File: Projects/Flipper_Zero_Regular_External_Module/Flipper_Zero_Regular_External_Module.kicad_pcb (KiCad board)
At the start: 2 copper layers, 67.5 x 19.8 mm, 2 parts, among them J1 Flipper_Zero

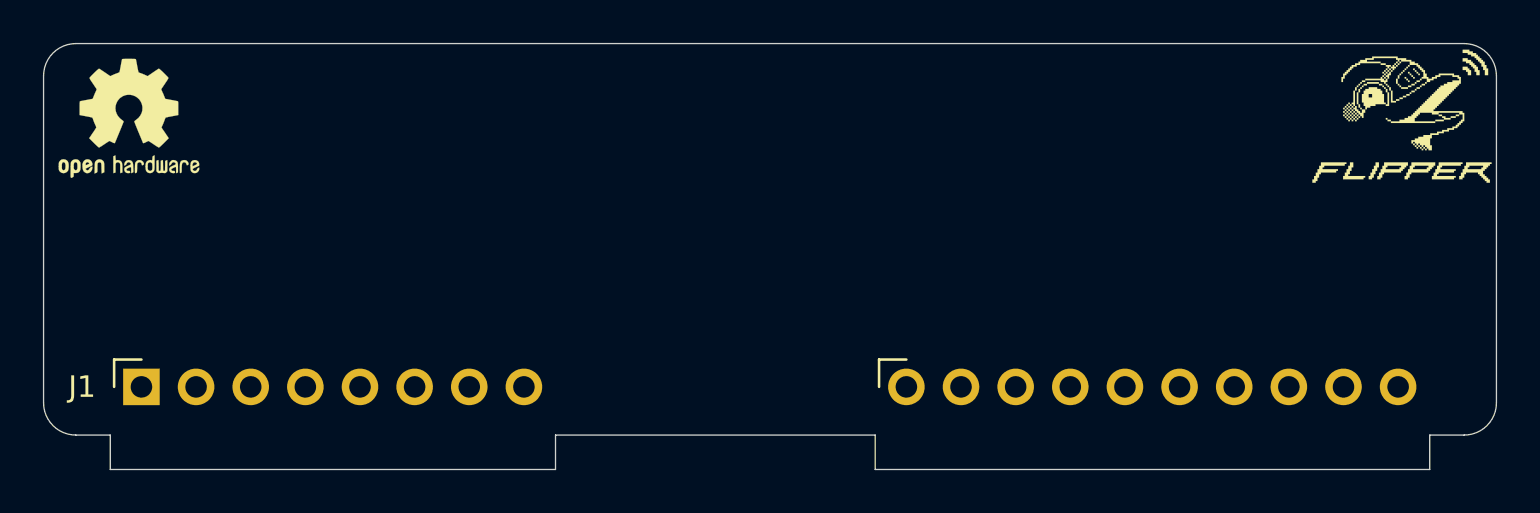
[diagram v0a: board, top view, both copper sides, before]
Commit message: Update to KiCAD 10
Signed-off-by: Ilias Daradimos <judgedrid@gmail.com>
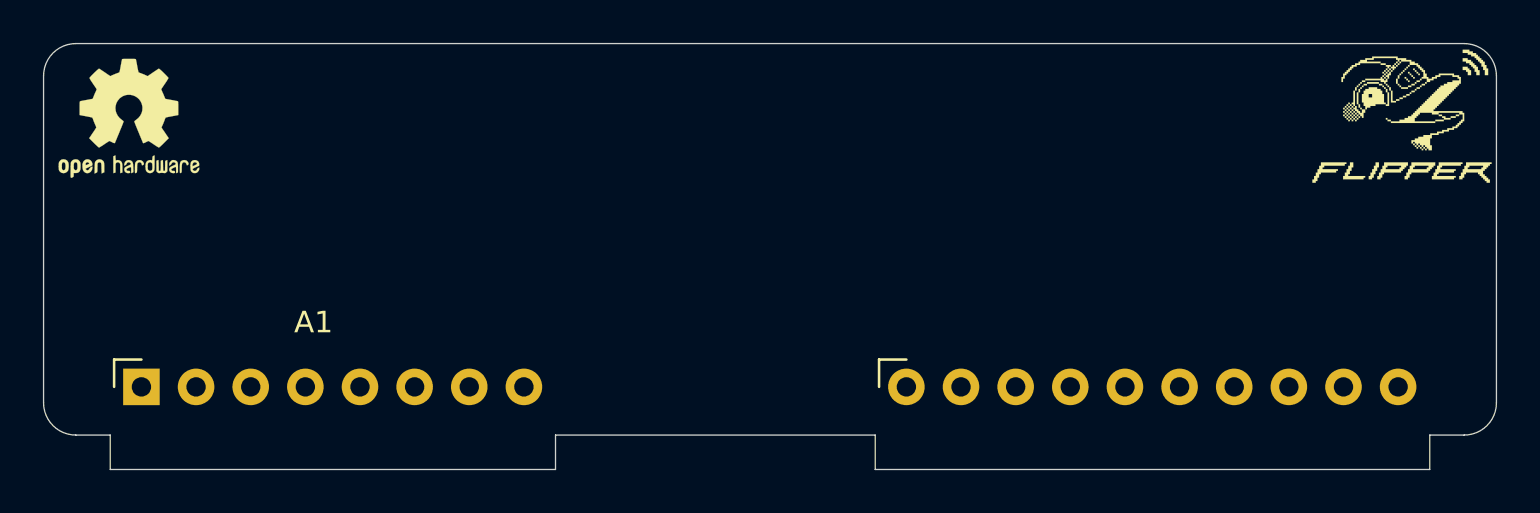
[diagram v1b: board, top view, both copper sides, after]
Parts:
- renumbered J1 to A1
